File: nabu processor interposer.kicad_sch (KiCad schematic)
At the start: 4 parts, among them J1 5V EXTRA, U1 LP3963-3.3

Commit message: begin integration of logic into atf1508
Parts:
- C1, C2: footprint (none) -> Capacitor_Tantalum_SMD:CP_EIA-3528-15_AVX-H
- J1: footprint (none) -> Connector_PinHeader_2.54mm:PinHeader_1x02_P2.54mm_Vertical
- U1: footprint (none) -> Package_TO_SOT_SMD:TO-263-5_TabPin3
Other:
- sheet BRAINS ports: added ~{RFSH}, ~{SYS}; removed none
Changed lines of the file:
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@@
     (property "Reference" "U1" (id 0) (at 213.36 138.43 0))
     (property "Value" "LP3963-3.3" (id 1) (at 213.36 140.97 0))
-    (property "Footprint" "" (id 2) (at 213.36 148.59 0)
+    (property "Footprint" "Package_TO_SOT_SMD:TO-263-5_TabPin3" (id 2) (at 213.36 148.59 0)
       (effects (font (size 1.27 1.27)) hide)
     )
@@
       (effects (font (size 1.27 1.27)) (justify left))
     )
-    (property "Footprint" "" (id 2) (at 262.89 153.67 0)
+    (property "Footprint" "Connector_PinHeader_2.54mm:PinHeader_1x02_P2.54mm_Vertical" (id 2) (at 262.89 153.67 0)
       (effects (font (size 1.27 1.27)) hide)
     )
@@
       (effects (font (size 1.27 1.27)) (justify left))
     )
-    (property "Footprint" "" (id 2) (at 231.14 151.13 0)
+    (property "Footprint" "Capacitor_Tantalum_SMD:CP_EIA-3528-15_AVX-H" (id 2) (at 231.14 151.13 0)
       (effects (font (size 1.27 1.27)) hide)
     )
@@
       (effects (font (size 1.27 1.27)) (justify left))
     )
-    (property "Footprint" "" (id 2) (at 193.04 151.13 0)
+    (property "Footprint" "Capacitor_Tantalum_SMD:CP_EIA-3528-15_AVX-H" (id 2) (at 193.04 151.13 0)
       (effects (font (size 1.27 1.27)) hide)
     )
@@
     (pin "DB[0..7]" bidirectional (at 63.5 66.04 180)
       (effects (font (size 1.27 1.27)) (justify left))
+    )
+    (pin "~{SYS}" input (at 63.5 53.34 180)
+      (effects (font (size 1.27 1.27)) (justify left))
+    )
+    (pin "~{RFSH}" output (at 88.9 45.72 0)
+      (effects (font (size 1.27 1.27)) (justify right))
     )
   )
@@
       (reference "#PWR0322") (unit 1) (value "GNDD") (footprint "")
     )
+    (path "/320705d8-4d7c-4302-8b3e-dbe54aa69e95/0f8ece08-65a5-4c8f-9f74-c1183875807a"
+      (reference "#PWR?") (unit 1) (value "GNDD") (footprint "")
+    )
+    (path "/320705d8-4d7c-4302-8b3e-dbe54aa69e95/4b0be4c5-db81-4d61-b2e8-d311632c350f"
+      (reference "#PWR?") (unit 1) (value "GNDD") (footprint "")
+    )
+    (path "/320705d8-4d7c-4302-8b3e-dbe54aa69e95/55dd29f1-bccc-4732-8255-1b2bf39caed5"
+      (reference "#PWR?") (unit 1) (value "+5V") (footprint "")
+    )
+    (path "/320705d8-4d7c-4302-8b3e-dbe54aa69e95/5b4e7db3-9a7b-4d94-9c0a-3b766cb31ff3"
+      (reference "#PWR?") (unit 1) (value "GNDD") (footprint "")
+    )
+    (path "/320705d8-4d7c-4302-8b3e-dbe54aa69e95/6f8baf8a-28a9-413d-9142-6cf1a8994adf"
+      (reference "#PWR?") (unit 1) (value "+5V") (footprint "")
+    )
+    (path "/320705d8-4d7c-4302-8b3e-dbe54aa69e95/74ecf149-cc35-4150-8b9a-fcf24f865b97"
+      (reference "#PWR?") (unit 1) (value "GNDD") (footprint "")
+    )
+    (path "/320705d8-4d7c-4302-8b3e-dbe54aa69e95/9ec5f3f5-c855-4a93-884e-c35b526be0b0"
+      (reference "#PWR?") (unit 1) (value "GNDD") (footprint "")
+    )
+    (path "/320705d8-4d7c-4302-8b3e-dbe54aa69e95/9f9fffa9-f707-4ae4-86b1-1de6d3ab243e"
+      (reference "#PWR?") (unit 1) (value "GNDD") (footprint "")
+    )
+    (path "/320705d8-4d7c-4302-8b3e-dbe54aa69e95/a38be6a6-6709-4e3b-94c6-1d07a7a47c07"
+      (reference "#PWR?") (unit 1) (value "+5V") (footprint "")
+    )
+    (path "/320705d8-4d7c-4302-8b3e-dbe54aa69e95/af0c3b39-f948-463b-b85a-f2b997d9ac96"
+      (reference "#PWR?") (unit 1) (value "GNDD") (footprint "")
+    )
+    (path "/320705d8-4d7c-4302-8b3e-dbe54aa69e95/cf6c44f9-ae33-4768-98b6-e9bf035b12a2"
+      (reference "#PWR?") (unit 1) (value "+5V") (footprint "")
+    )
+    (path "/320705d8-4d7c-4302-8b3e-dbe54aa69e95/d7f5ed70-e933-478e-bfdc-450d0e05c7a0"
+      (reference "#PWR?") (unit 1) (value "+5V") (footprint "")
+    )
+    (path "/320705d8-4d7c-4302-8b3e-dbe54aa69e95/dcec817c-a584-4dd8-9bbf-3c5b70201944"
+      (reference "#PWR?") (unit 1) (value "GNDD") (footprint "")
+    )
+    (path "/320705d8-4d7c-4302-8b3e-dbe54aa69e95/e7780d32-85a1-4157-ad52-2e42e94b28cd"
+      (reference "#PWR?") (unit 1) (value "GNDD") (footprint "")
+    )
+    (path "/320705d8-4d7c-4302-8b3e-dbe54aa69e95/f9353a2e-262c-4639-8e7c-675fee4a0117"
+      (reference "#PWR?") (unit 1) (value "+5V") (footprint "")
+    )
+    (path "/320705d8-4d7c-4302-8b3e-dbe54aa69e95/fff1e5d9-44d0-4aaa-92fd-20e1e171bf39"
+      (reference "#PWR?") (unit 1) (value "GNDD") (footprint "")
+    )
     (path "/ed39334a-848a-4da5-a2cc-a2eddeab4ea4"
       (reference "C1") (unit 1) (value "100U TANT") (footprint "Capacitor_Tantalum_SMD:CP_EIA-3528-15_AVX-H")
@@
       (reference "C38") (unit 1) (value "0U1") (footprint "Capacitor_SMD:C_0603_1608Metric")
     )
+    (path "/320705d8-4d7c-4302-8b3e-dbe54aa69e95/718520aa-c12a-4fff-b041-a6ca5784dded"
+      (reference "C?") (unit 1) (value "0U1") (footprint "Capacitor_SMD:C_1206_3216Metric")
+    )
+    (path "/320705d8-4d7c-4302-8b3e-dbe54aa69e95/f8d511c4-fa04-4f04-9035-33c00c00c2bc"
+      (reference "C?") (unit 1) (value "0U1") (footprint "Capacitor_SMD:C_1206_3216Metric")
+    )
     (path "/bfed3eaf-37d2-442e-8baa-ce241bc80bc3/222c9f64-d02f-44cc-a35f-64a1b4ae84b7"
       (reference "D1") (unit 1) (value "BAT48JFILM") (footprint "Diode_SMD:D_SOD-323")
@@
       (reference "U74") (unit 1) (value "74LVC1G332") (footprint "Package_TO_SOT_SMD:SOT-363_SC-70-6")
     )
-  )
+    (path "/320705d8-4d7c-4302-8b3e-dbe54aa69e95/5e1ccda5-a997-475c-a565-10e978d13def"
+      (reference "U?") (unit 1) (value "74HC245") (footprint "")
+    )
+    (path "/320705d8-4d7c-4302-8b3e-dbe54aa69e95/91e7e6ed-6011-4433-ae7c-0361915708f8"
+      (reference "U?") (unit 1) (value "74HC245") (footprint "")
+    )
+    (path "/320705d8-4d7c-4302-8b3e-dbe54aa69e95/c842e4bb-545a-40bf-94ca-429823194d9b"
+      (reference "U?") (unit 1) (value "74HC245") (footprint "")
+    )
+    (path "/320705d8-4d7c-4302-8b3e-dbe54aa69e95/f6192cdc-45d6-42b7-9bfa-a2eb86d8f3bd"
+      (reference "U?") (unit 1) (value "74HC245") (footprint "")
+    )
+  )

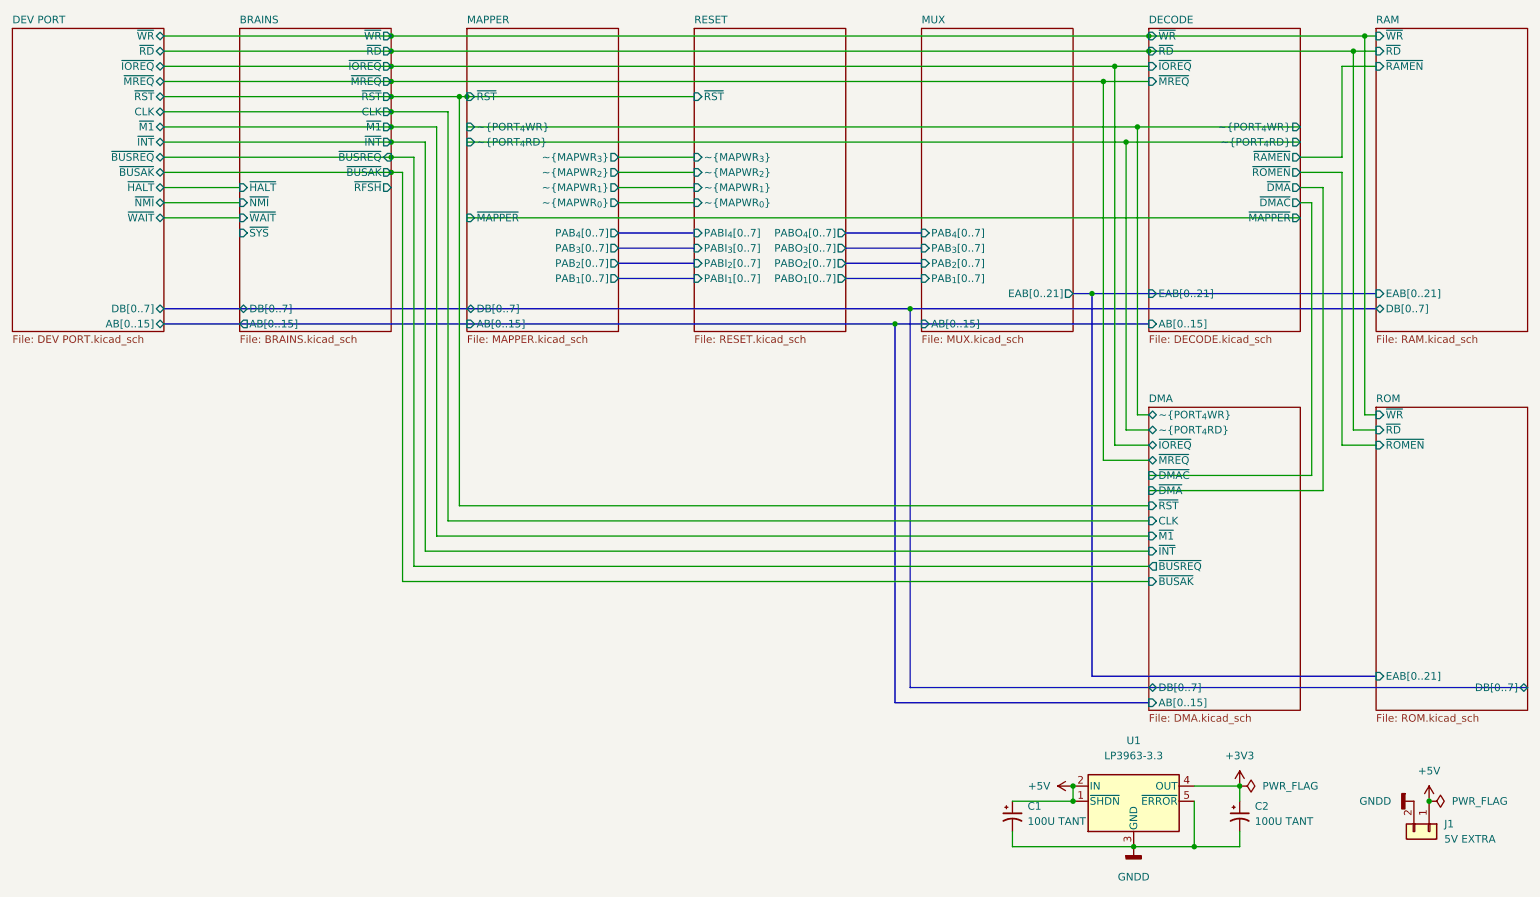
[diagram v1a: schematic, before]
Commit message: added ATF150x part (specifically the 1508) vhdl file contains the (hopeful) implementition of the mapper
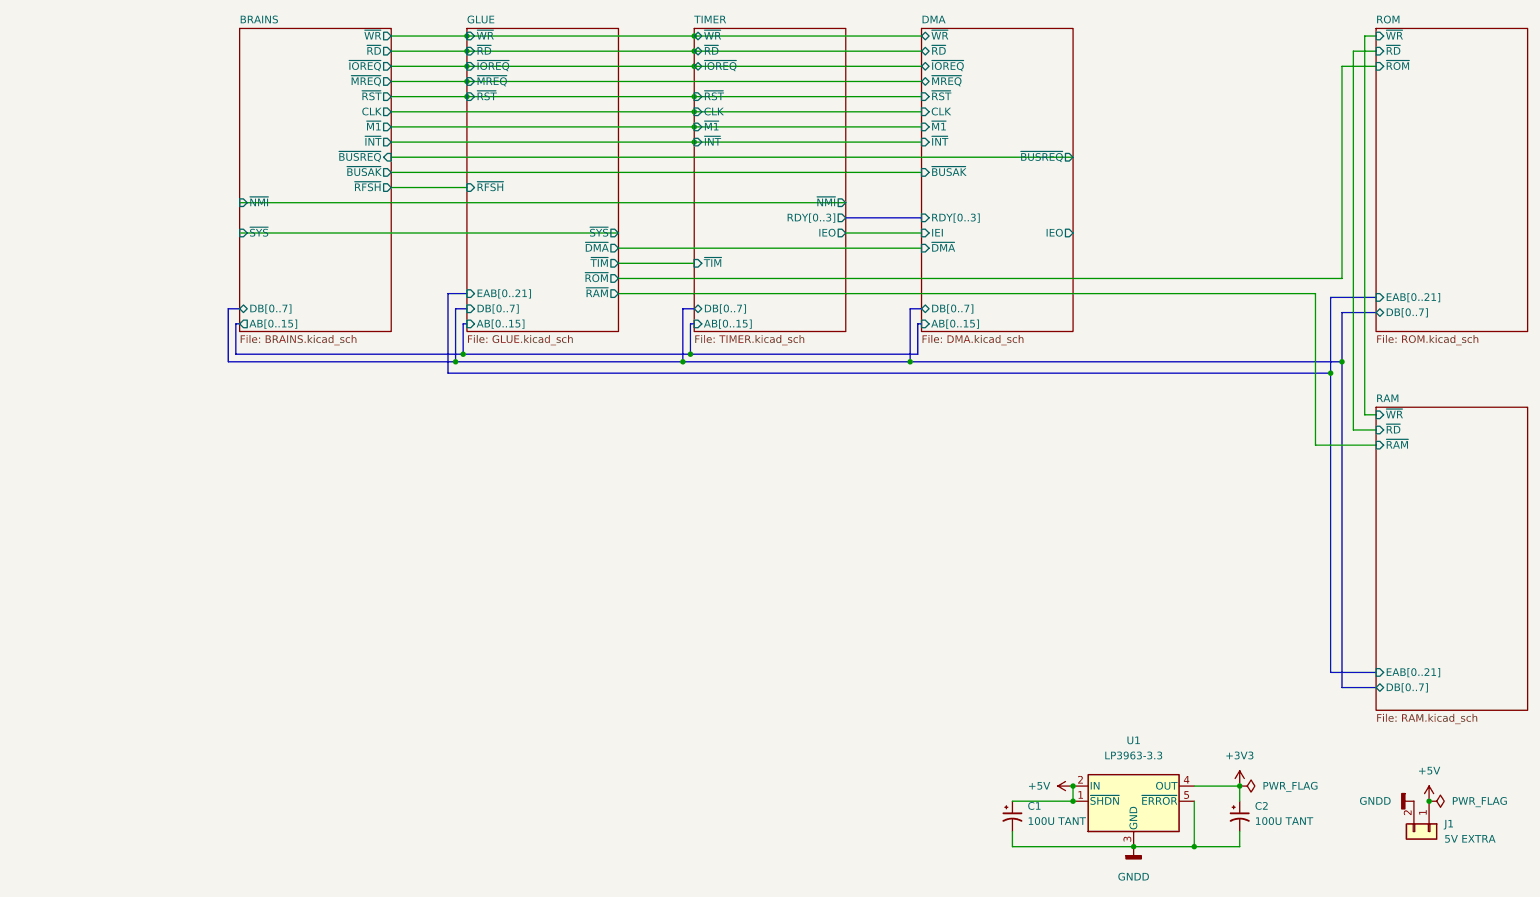
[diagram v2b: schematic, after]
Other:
- removed sheet DECODE
- removed sheet DEV PORT
- removed sheet MAPPER
- removed sheet MUX
- removed sheet RESET
- added sheet GLUE (GLUE.kicad_sch)
- added sheet TIMER (TIMER.kicad_sch)
- sheet BRAINS ports: added none; removed ~{HALT}, ~{WAIT}
- sheet DMA ports: added IEI, IEO, RDY[0..3], ~{RD}, ~{WR}; removed ~{DMAC}, ~{PORT_{4}RD}, ~{PORT_{4}WR}
- sheet RAM ports: added ~{RAM}; removed ~{RAMEN}
- sheet ROM ports: added ~{ROM}; removed ~{ROMEN}

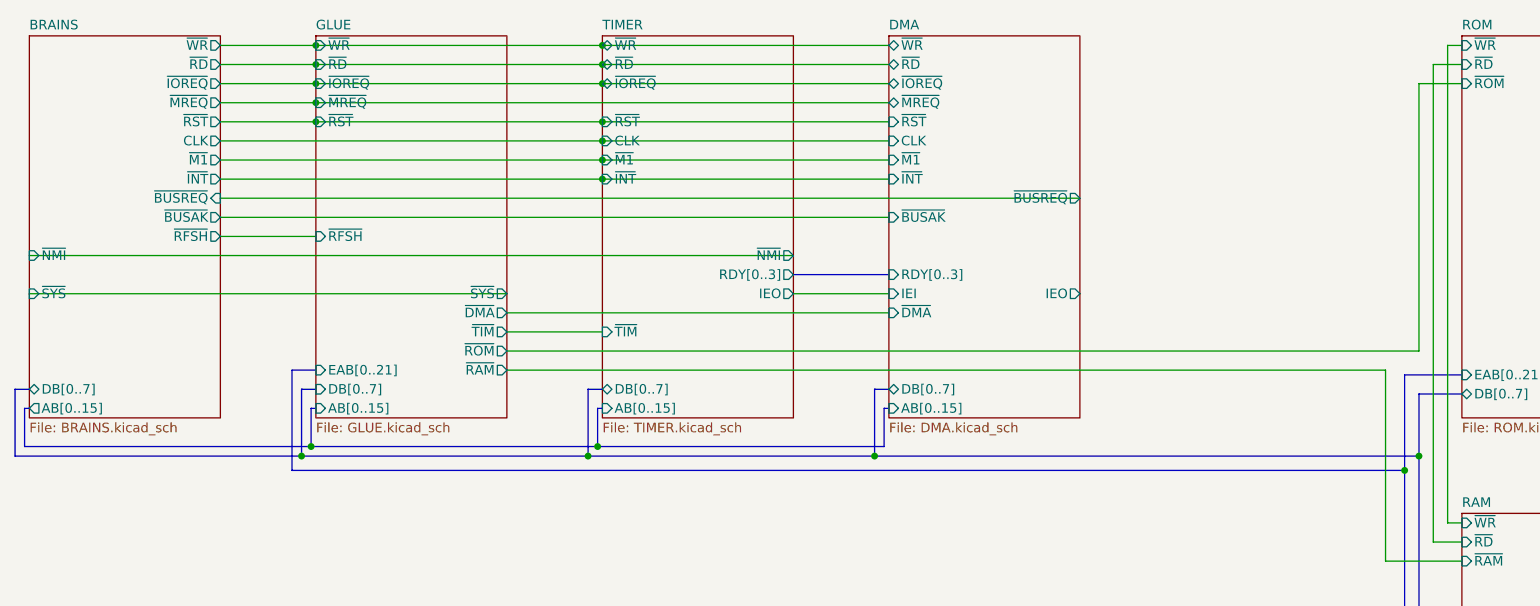
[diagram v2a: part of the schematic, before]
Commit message: updated 84c10 pinout, apparently never checked for validity.... further simplification of dma and timer system (removed mode 2 interrupt structure, and interrupts in general) cleaned up vhdl code for 1508, still need testing to ensure functionality and that it even fits in the 1508....
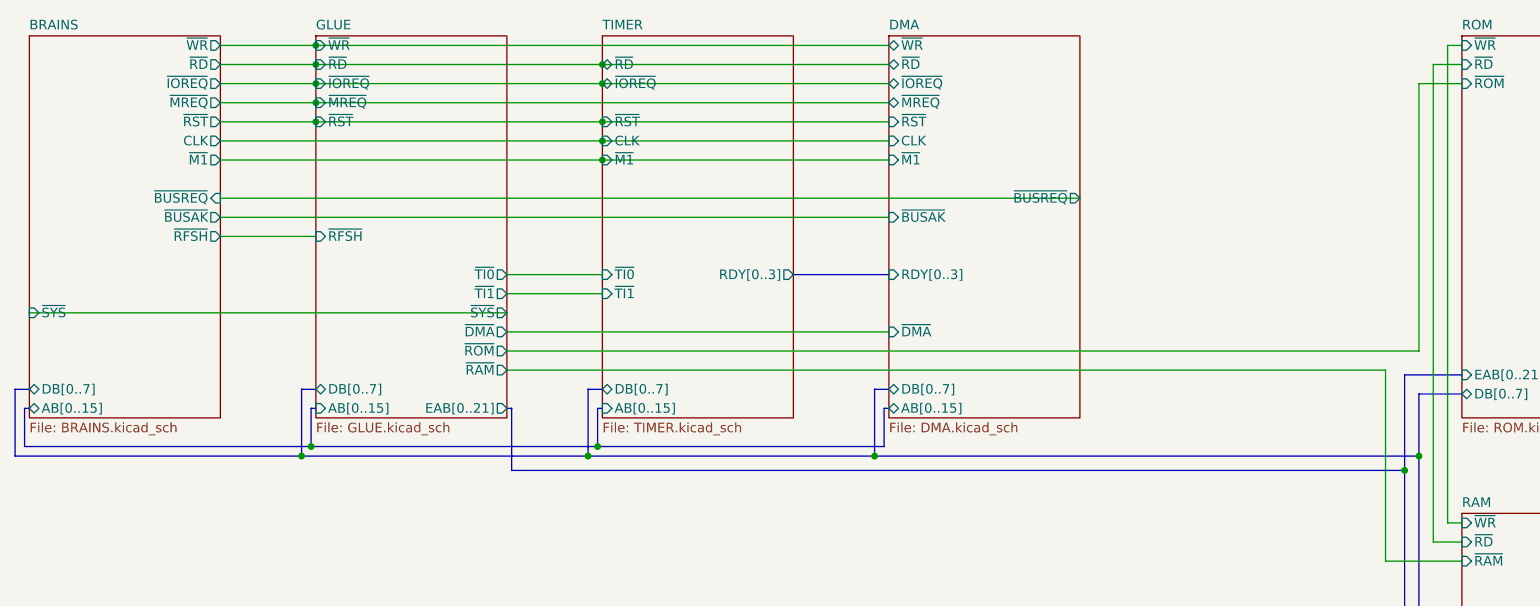
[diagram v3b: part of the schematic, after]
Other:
- sheet BRAINS ports: added none; removed ~{INT}, ~{NMI}
- sheet DMA ports: added none; removed IEI, IEO, ~{INT}
- sheet GLUE ports: added ~{TI0}, ~{TI1}; removed ~{TIM}
- sheet TIMER ports: added ~{TI0}, ~{TI1}; removed IEO, ~{INT}, ~{NMI}, ~{TIM}, ~{WR}

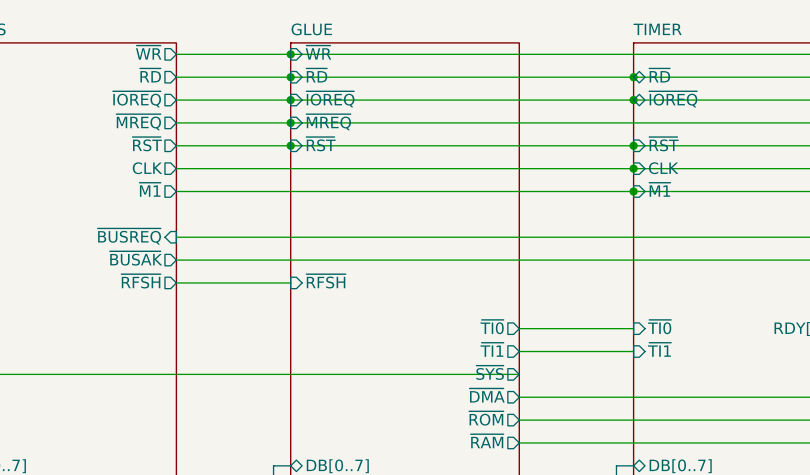
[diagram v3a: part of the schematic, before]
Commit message: forgot to actually add the previous fixes to kicad
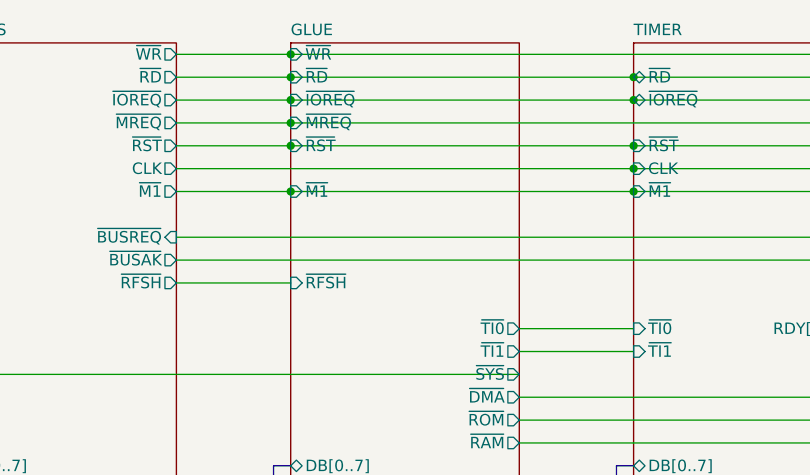
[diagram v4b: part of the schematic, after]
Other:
- sheet GLUE ports: added ~{M1}; removed none
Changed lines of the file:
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@@
   (junction (at 101.6 20.32) (diameter 0) (color 0 0 0 0)
   )
+  (junction (at 101.6 35.56) (diameter 0) (color 0 0 0 0)
+  )
   (junction (at 213.36 156.21) (diameter 0) (color 0 0 0 0)
   )
@@
     (stroke (width 0) (type default) (color 0 0 0 0))
   )
-  (wire (pts (xy 88.9 35.56) (xy 139.7 35.56))
+  (wire (pts (xy 88.9 35.56) (xy 101.6 35.56))
     (stroke (width 0) (type default) (color 0 0 0 0))
   )
@@
   )
   (bus (pts (xy 99.695 74.93) (xy 99.695 66.04))
+    (stroke (width 0) (type default) (color 0 0 0 0))
+  )
+  (wire (pts (xy 101.6 35.56) (xy 139.7 35.56))
     (stroke (width 0) (type default) (color 0 0 0 0))
   )
@@
       (effects (font (size 1.27 1.27)) (justify right))
     )
-  )
+    (pin "~{M1}" input (at 101.6 35.56 180)
+      (effects (font (size 1.27 1.27)) (justify left))
+    )
+  )

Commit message: fixed logic errors (me being dumb forgetting associativity of ops, and fixed write only system databus on interposer
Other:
- sheet BRAINS ports: added DIR; removed none
- sheet GLUE ports: added DIR; removed none
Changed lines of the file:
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@@
+    (stroke (width 0) (type default) (color 0 0 0 0))
+  )
+  (wire (pts (xy 63.5 38.1) (xy 127 38.1))
     (stroke (width 0) (type default) (color 0 0 0 0))
   )
@@
       (effects (font (size 1.27 1.27)) (justify right))
     )
+    (pin "DIR" input (at 63.5 38.1 180)
+      (effects (font (size 1.27 1.27)) (justify left))
+    )
   )
   (sheet (at 177.8 19.05) (size 25.4 50.8) (fields_autoplaced)
@@
     (pin "~{M1}" input (at 101.6 35.56 180)
       (effects (font (size 1.27 1.27)) (justify left))
+    )
+    (pin "DIR" tri_state (at 127 38.1 0)
+      (effects (font (size 1.27 1.27)) (justify right))
     )
   )
@@
       (reference "#PWR066") (unit 1) (value "+5V") (footprint "")
     )
-    (path "/320705d8-4d7c-4302-8b3e-dbe54aa69e95/e7780d32-85a1-4157-ad52-2e42e94b28cd"
-      (reference "#PWR067") (unit 1) (value "GNDD") (footprint "")
-    )
     (path "/320705d8-4d7c-4302-8b3e-dbe54aa69e95/f0bd75ac-bfa3-4ab3-a163-f5074bbe7860"
